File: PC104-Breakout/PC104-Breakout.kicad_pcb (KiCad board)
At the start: 4 copper layers, 150 x 100 mm, 17 parts, among them J1 Screw_Terminal_01x02, J2 Screw_Terminal_01x02, J3 Screw_Terminal_01x02, M1 MountingHole_Pad, M2 MountingHole_Pad, M3 MountingHole_Pad, M4 MountingHole_Pad, M5 MountingHole_Pad, M6 MountingHole_Pad, M7 MountingHole_Pad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

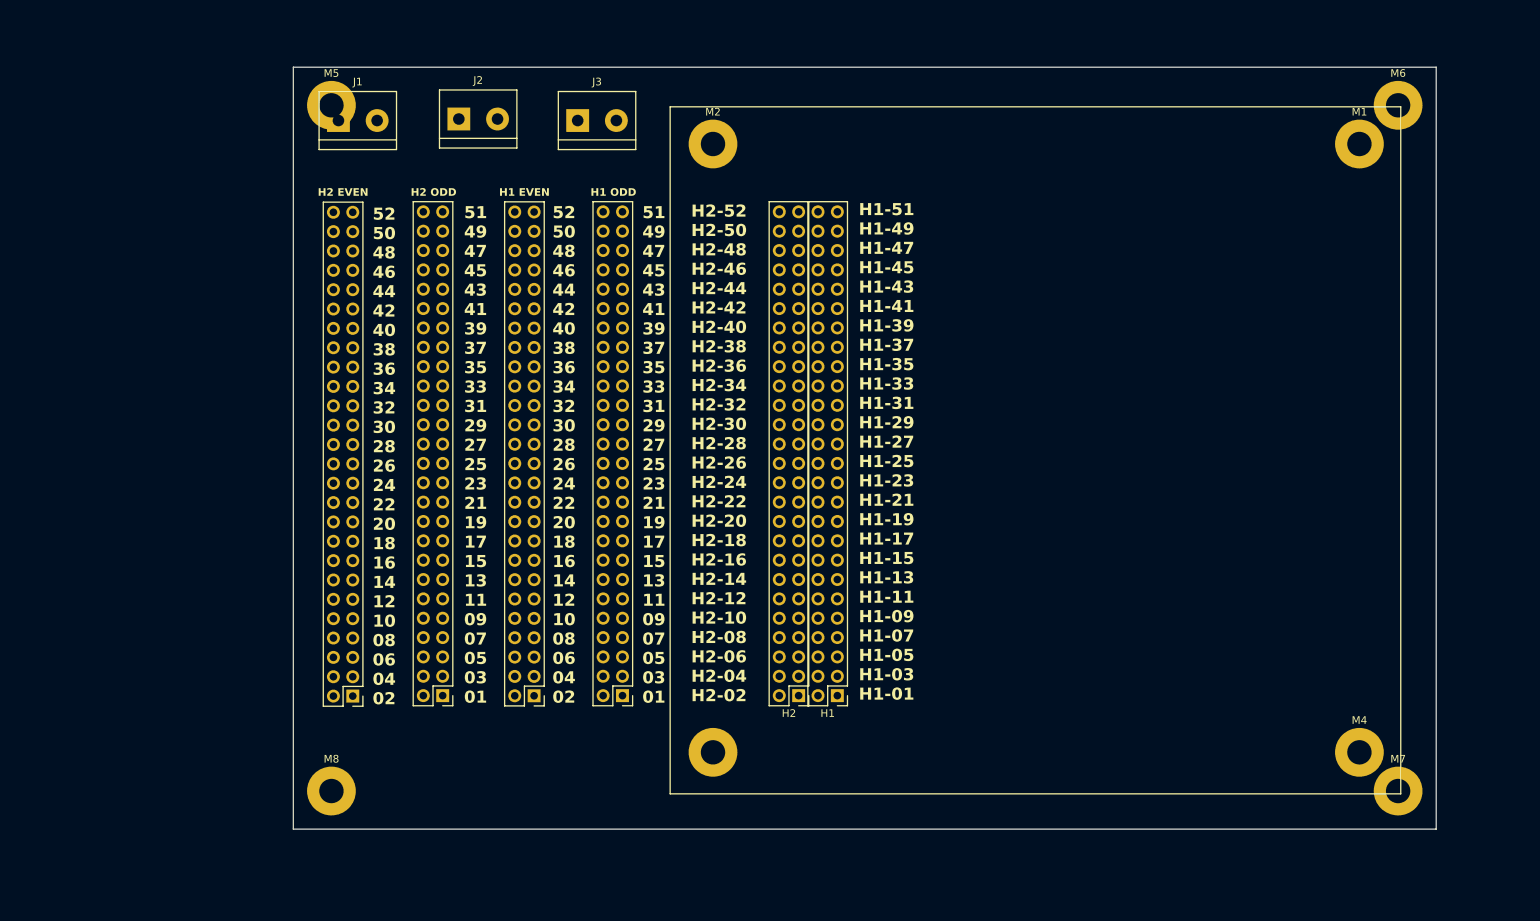
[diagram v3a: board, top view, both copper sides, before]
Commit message: Intense layout/positioning of the PC104 spec
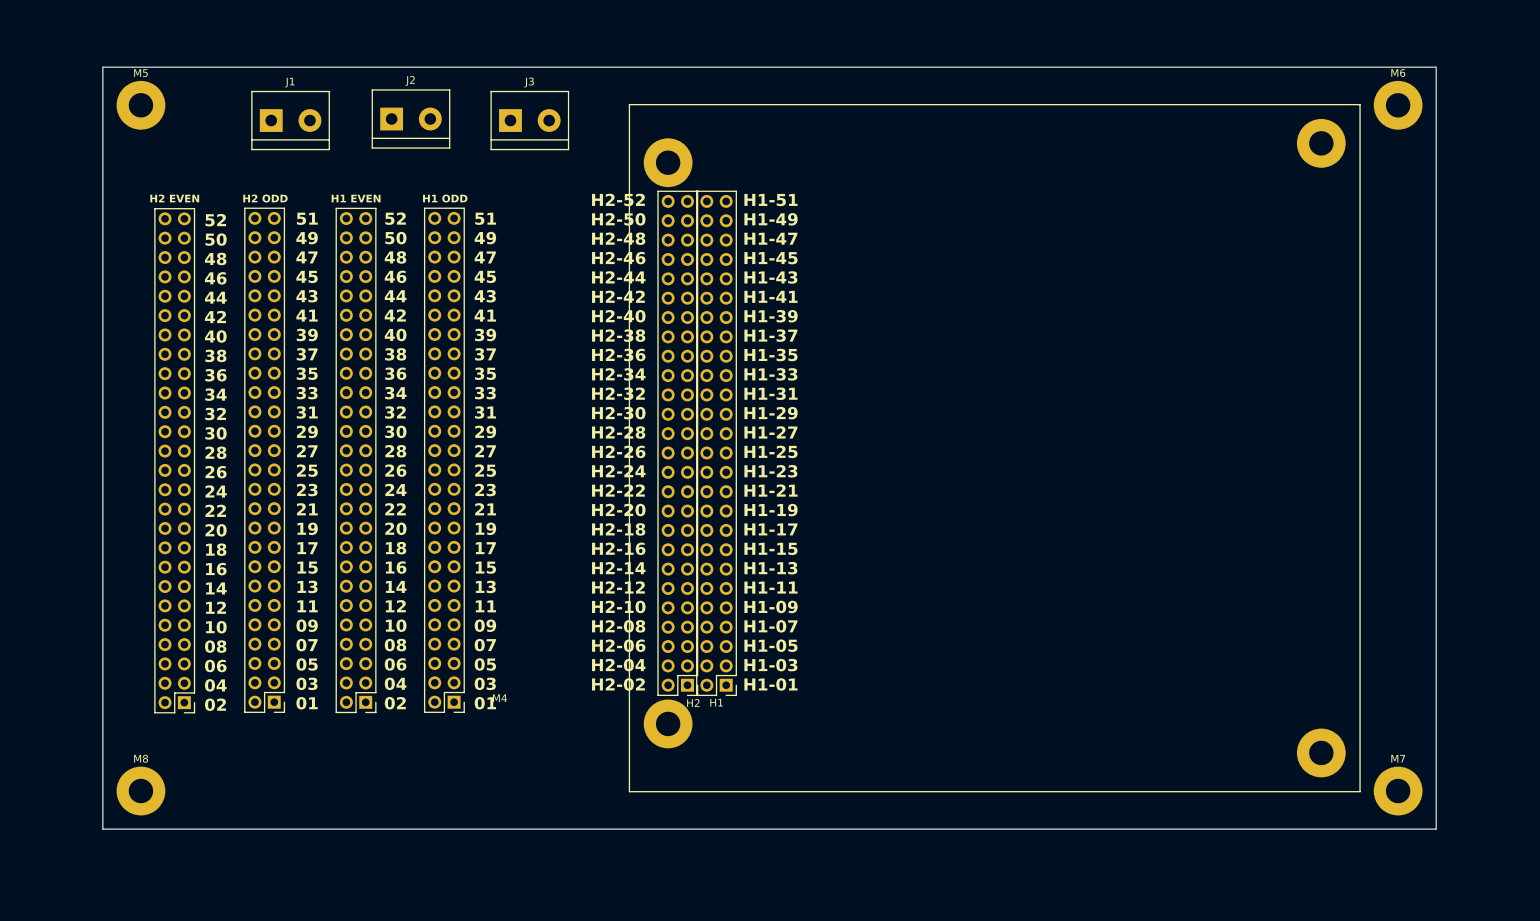
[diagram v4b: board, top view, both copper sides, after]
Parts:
- moved M4 90.8 mm to (149.2, 136.2)
- moved M1 90.8 mm to (149.2, 62.5)
- moved M2 79.8 mm to (234.9, 60.0)
- moved M3 79.8 mm to (234.9, 140.0)
- moved M5 25.0 mm to (80.0, 55.0)
- moved M8 25.0 mm to (80.0, 145.0)
- moved H1E1 22.1 mm to (109.5, 133.4)
- moved H1O1 22.1 mm to (121.1, 133.3)
- moved H2E1 22.1 mm to (85.7, 133.4)
- moved H2O1 22.1 mm to (97.5, 133.3)
- moved H1 14.7 mm to (156.8, 131.1)
- moved H2 14.7 mm to (151.7, 131.1)
- moved J1 8.82 mm to (97.1, 57.0)
- moved J2 8.82 mm to (112.9, 56.8)
- moved J3 8.82 mm to (128.5, 57.0)
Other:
- board size 150 x 100 mm -> 175 x 100 mm
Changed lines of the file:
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@@
 		(legacy_teardrops no)
 	)
-	(paper "A4")
+	(paper "USLetter")
 	(layers
 		(0 "F.Cu" signal)
@@
 	(footprint "Connector_PinHeader_2.54mm:PinHeader_2x26_P2.54mm_Vertical"
 		(layer "F.Cu")
-		(at 131.6 132.5 180)
+		(at 109.5 133.36 180)
 		(descr "Through hole straight pin header, 2x26, 2.54mm pitch, double rows")
 		(tags "Through hole pin header THT 2x26 2.54mm double row")
@@
 	)
 	(footprint "Connector_PinHeader_2.54mm:PinHeader_2x26_P2.54mm_Vertical"
+		(locked yes)
 		(layer "F.Cu")
-		(at 171.4 132.48 180)
+		(at 156.81 131.115 180)
 		(descr "Through hole straight pin header, 2x26, 2.54mm pitch, double rows")
 		(tags "Through hole pin header THT 2x26 2.54mm double row")
@@
 	)
 	(footprint "MountingHole:MountingHole_3.2mm_M3_Pad"
+		(locked yes)
 		(layer "F.Cu")
-		(at 155.08 60.08)
+		(at 234.92 59.995)
 		(descr "Mounting Hole 3.2mm, M3")
 		(tags "mounting hole 3.2mm m3")
@@
 			(at 0 -4.2 0)
 			(layer "F.SilkS")
+			(hide yes)
 			(effects
 				(font
@@
 	)
 	(footprint "MountingHole:MountingHole_3.2mm_M3_Pad"
+		(locked yes)
 		(layer "F.Cu")
-		(at 155.08 139.92)
+		(at 234.92 140.005)
 		(descr "Mounting Hole 3.2mm, M3")
 		(tags "mounting hole 3.2mm m3")
@@
 	(footprint "Connector_PinHeader_2.54mm:PinHeader_2x26_P2.54mm_Vertical"
 		(layer "F.Cu")
-		(at 143.2 132.48 180)
+		(at 121.1 133.34 180)
 		(descr "Through hole straight pin header, 2x26, 2.54mm pitch, double rows")
 		(tags "Through hole pin header THT 2x26 2.54mm double row")
@@
 	(footprint "TerminalBlock:TerminalBlock_bornier-2_P5.08mm"
 		(layer "F.Cu")
-		(at 105.92 57)
+		(at 97.1 57)
 		(descr "simple 2-pin terminal block, pitch 5.08mm, revamped version of bornier2")
 		(tags "terminal block bornier2")
@@
 	)
 	(footprint "MountingHole:MountingHole_3.2mm_M3_Pad"
+		(locked yes)
 		(layer "F.Cu")
-		(at 239.92 139.92)
+		(at 149.19 136.195)
 		(descr "Mounting Hole 3.2mm, M3")
 		(tags "mounting hole 3.2mm m3")
 		(property "Reference" "M4"
-			(at 0 -4.2 0)
+			(at -22.1 -3.34 0)
 			(layer "F.SilkS")
 			(effects
@@
 	)
 	(footprint "MountingHole:MountingHole_3.2mm_M3_Pad"
+		(locked yes)
 		(layer "F.Cu")
 		(at 245 55)
@@
 	(footprint "MountingHole:MountingHole_3.2mm_M3_Pad"
 		(layer "F.Cu")
-		(at 105 55)
+		(at 80 55)
 		(descr "Mounting Hole 3.2mm, M3")
 		(tags "mounting hole 3.2mm m3")
@@
 	)
 	(footprint "MountingHole:MountingHole_3.2mm_M3_Pad"
+		(locked yes)
 		(layer "F.Cu")
-		(at 239.92 60.08)
+		(at 149.19 62.535)
 		(descr "Mounting Hole 3.2mm, M3")
 		(tags "mounting hole 3.2mm m3")
@@
 			(at 0 -4.2 0)
 			(layer "F.SilkS")
+			(hide yes)
 			(effects
 				(font
@@
 	(footprint "Connector_PinHeader_2.54mm:PinHeader_2x26_P2.54mm_Vertical"
 		(layer "F.Cu")
-		(at 119.6 132.48 180)
+		(at 97.5 133.34 180)
 		(descr "Through hole straight pin header, 2x26, 2.54mm pitch, double rows")
 		(tags "Through hole pin header THT 2x26 2.54mm double row")
@@
 	(footprint "MountingHole:MountingHole_3.2mm_M3_Pad"
 		(layer "F.Cu")
-		(at 105 145)
+		(at 80 145)
 		(descr "Mounting Hole 3.2mm, M3")
 		(tags "mounting hole 3.2mm m3")
@@
 	(footprint "TerminalBlock:TerminalBlock_bornier-2_P5.08mm"
 		(layer "F.Cu")
-		(at 137.32 57)
+		(at 128.5 57)
 		(descr "simple 2-pin terminal block, pitch 5.08mm, revamped version of bornier2")
 		(tags "terminal block bornier2")
@@
 	(footprint "TerminalBlock:TerminalBlock_bornier-2_P5.08mm"
 		(layer "F.Cu")
-		(at 121.72 56.8)
+		(at 112.9 56.8)
 		(descr "simple 2-pin terminal block, pitch 5.08mm, revamped version of bornier2")
 		(tags "terminal block bornier2")
@@
 	)
 	(footprint "Connector_PinHeader_2.54mm:PinHeader_2x26_P2.54mm_Vertical"
+		(locked yes)
 		(layer "F.Cu")
-		(at 166.32 132.48 180)
+		(at 151.73 131.115 180)
 		(descr "Through hole straight pin header, 2x26, 2.54mm pitch, double rows")
 		(tags "Through hole pin header THT 2x26 2.54mm double row")
 		(property "Reference" "H2"
-			(at 1.27 -2.33 180)
+			(at -0.77 -2.385 180)
 			(layer "F.SilkS")
 			(effects
@@
 	)
 	(footprint "MountingHole:MountingHole_3.2mm_M3_Pad"
+		(locked yes)
 		(layer "F.Cu")
 		(at 245 145)
@@
 	(footprint "Connector_PinHeader_2.54mm:PinHeader_2x26_P2.54mm_Vertical"
 		(layer "F.Cu")
-		(at 107.8 132.54 180)
+		(at 85.7 133.4 180)
 		(descr "Through hole straight pin header, 2x26, 2.54mm pitch, double rows")
 		(tags "Through hole pin header THT 2x26 2.54mm double row")
@@
 	)
 	(gr_rect
-		(start 149.455 55.2)
-		(end 245.345 145.37)
+		(start 144.11 54.915)
+		(end 240 145.085)
+		(locked yes)
 		(stroke
 			(width 0.1)
@@
 	)
 	(gr_rect
-		(start 100 50)
+		(start 75 50)
 		(end 250 150)
 		(stroke
@@
 	)
 	(gr_text "52\n50\n48\n46\n44\n42\n40\n38\n36\n34\n32\n30\n28\n26\n24\n22\n20\n18\n16\n14\n12\n10\n08\n06\n04\n02"
-		(at 110.4 133.8 0)
+		(at 88.3 134.66 0)
 		(layer "F.SilkS")
 		(effects
@@
 	)
 	(gr_text "52\n50\n48\n46\n44\n42\n40\n38\n36\n34\n32\n30\n28\n26\n24\n22\n20\n18\n16\n14\n12\n10\n08\n06\n04\n02"
-		(at 134 133.6 0)
+		(at 111.9 134.46 0)
 		(layer "F.SilkS")
 		(effects
@@
 	)
 	(gr_text "H2 EVEN\n"
-		(at 103.2 67 0)
+		(at 81.1 67.86 0)
 		(layer "F.SilkS")
 		(effects
@@
 	)
 	(gr_text "H1 EVEN\n"
-		(at 127 67 0)
+		(at 104.9 67.86 0)
 		(layer "F.SilkS")
 		(effects
@@
 	)
 	(gr_text "H1-51\nH1-49\nH1-47\nH1-45\nH1-43\nH1-41\nH1-39\nH1-37\nH1-35\nH1-33\nH1-31\nH1-29\nH1-27\nH1-25\nH1-23\nH1-21\nH1-19\nH1-17\nH1-15\nH1-13\nH1-11\nH1-09\nH1-07\nH1-05\nH1-03\nH1-01"
-		(at 174.2 133.2 0)
+		(locked yes)
+		(at 159 132 0)
 		(layer "F.SilkS")
 		(effects
@@
 	)
 	(gr_text "H1 ODD"
-		(at 139 67 0)
+		(at 116.9 67.86 0)
 		(layer "F.SilkS")
 		(effects
@@
 	)
 	(gr_text "51\n49\n47\n45\n43\n41\n39\n37\n35\n33\n31\n29\n27\n25\n23\n21\n19\n17\n15\n13\n11\n09\n07\n05\n03\n01"
-		(at 145.8 133.6 0)
+		(at 123.7 134.46 0)
 		(layer "F.SilkS")
 		(effects
@@
 	)
 	(gr_text "H2 ODD"
-		(at 115.4 67 0)
+		(at 93.3 67.86 0)
 		(layer "F.SilkS")
 		(effects
@@
 	)
 	(gr_text "51\n49\n47\n45\n43\n41\n39\n37\n35\n33\n31\n29\n27\n25\n23\n21\n19\n17\n15\n13\n11\n09\n07\n05\n03\n01"
-		(at 122.4 133.6 0)
+		(at 100.3 134.46 0)
 		(layer "F.SilkS")
 		(effects
@@
 	)
 	(gr_text "H2-52\nH2-50\nH2-48\nH2-46\nH2-44\nH2-42\nH2-40\nH2-38\nH2-36\nH2-34\nH2-32\nH2-30\nH2-28\nH2-26\nH2-24\nH2-22\nH2-20\nH2-18\nH2-16\nH2-14\nH2-12\nH2-10\nH2-08\nH2-06\nH2-04\nH2-02"
-		(at 152.2 133.4 0)
+		(locked yes)
+		(at 139 132 0)
 		(layer "F.SilkS")
 		(effects

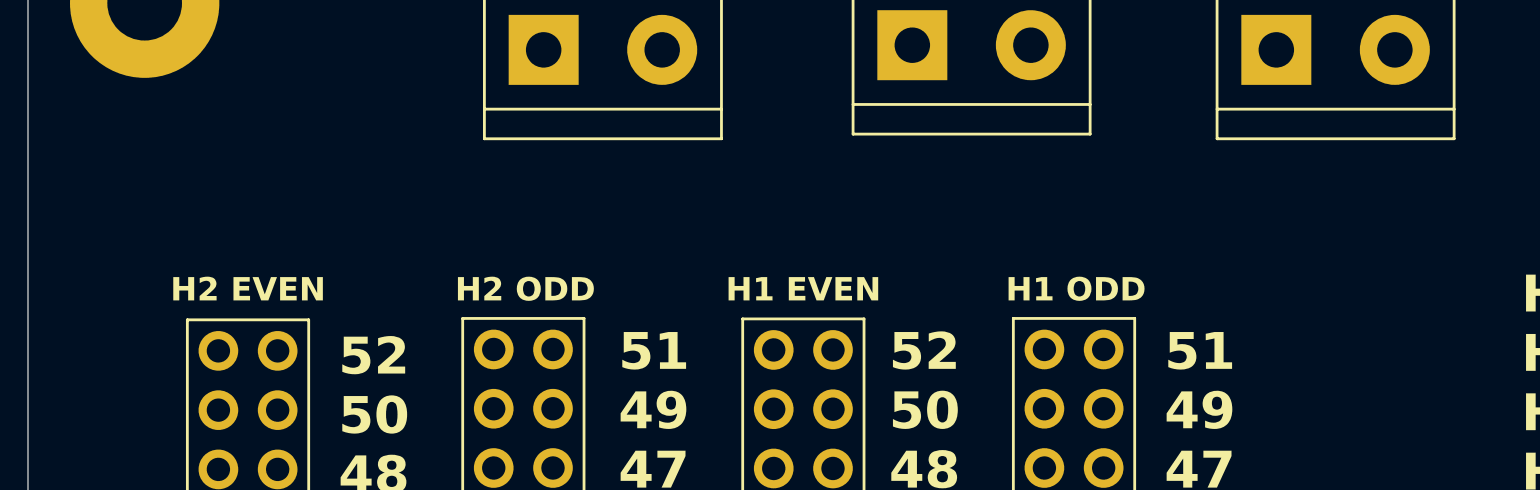
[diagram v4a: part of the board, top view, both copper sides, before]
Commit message: Added 3.3V and GND LEDs
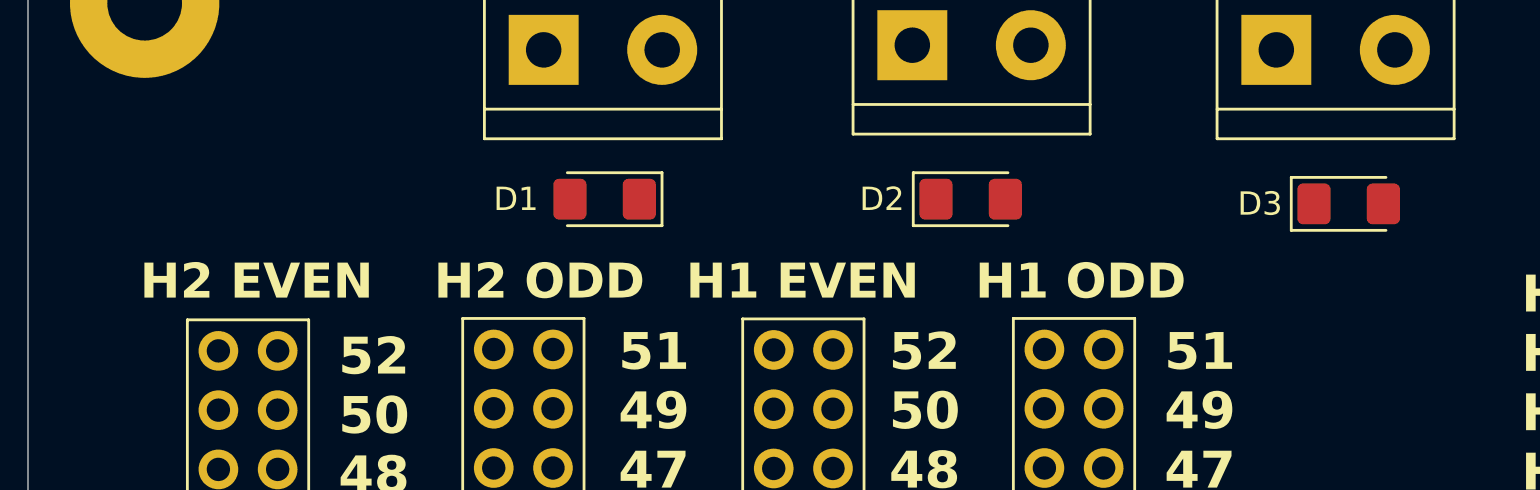
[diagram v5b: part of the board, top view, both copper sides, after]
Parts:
- added D1: D, Diode_SMD:D_1206_3216Metric_Pad1.42x1.75mm_HandSolder, F.Cu at (99.7, 63.4)
- added D2: D, Diode_SMD:D_1206_3216Metric_Pad1.42x1.75mm_HandSolder, F.Cu at (115.4, 63.4)
- added D3: D, Diode_SMD:D_1206_3216Metric_Pad1.42x1.75mm_HandSolder, F.Cu at (131.6, 63.6)
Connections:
- J1 pad 1: H2-29 -> Net-(D1-A)
- J1 pad 2: H2-29 -> Net-(D1-A)
- J2 pad 1: H2-25 -> Net-(D2-A)
- J2 pad 2: H2-25 -> Net-(D2-A)
- J3 pad 1: H2-27 -> Net-(D3-A)
- J3 pad 2: H2-27 -> Net-(D3-A)
